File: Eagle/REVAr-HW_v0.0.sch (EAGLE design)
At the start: 104 parts, among them IC1 MC33269ST-5.0T3, IC2 MC33269D-5.0, IC3 ATMEGA2560-16AU, IC4 ATMEGA8U2-MU, IC5 LM358D, IC6 LP2985-33DBVR, IC7 PCF8574T, Q1 16MHz, Q2 16MHz, T2 FDN340P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

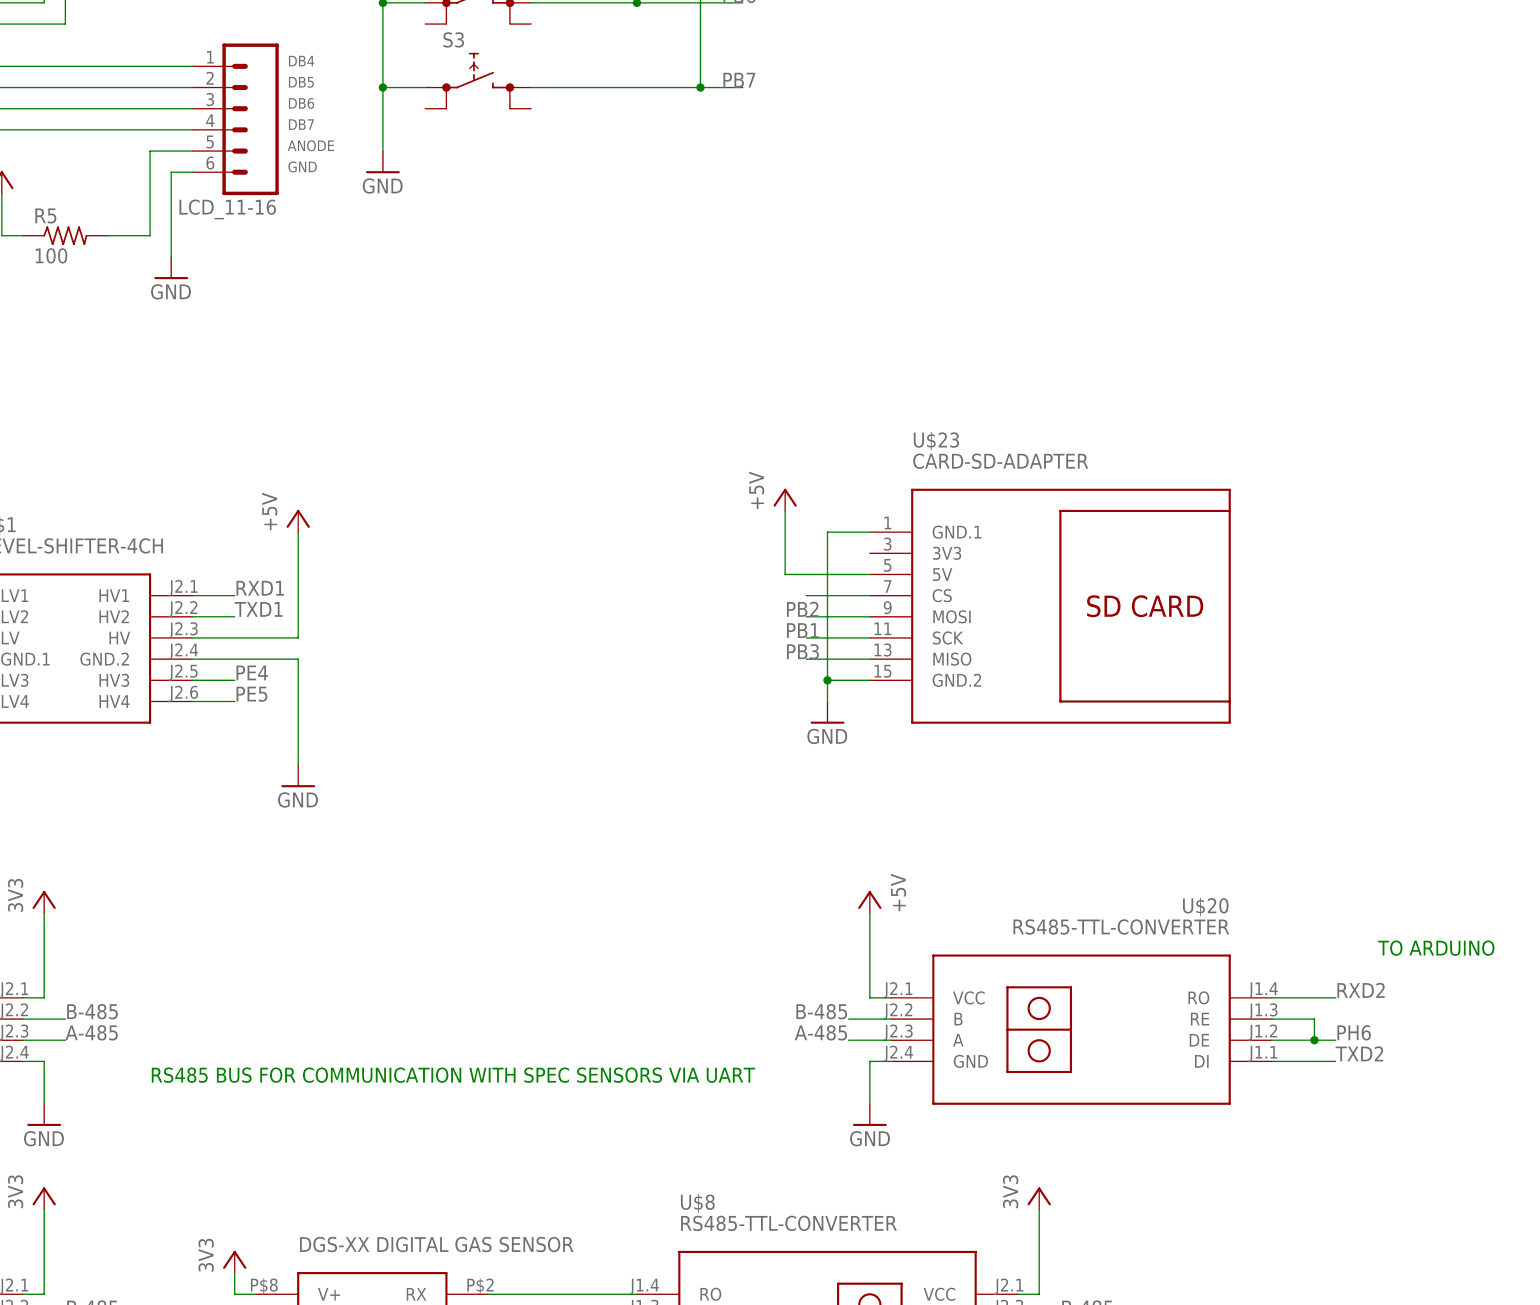
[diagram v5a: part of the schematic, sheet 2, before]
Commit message: [HW] Add BMP280 and DS1307 to design
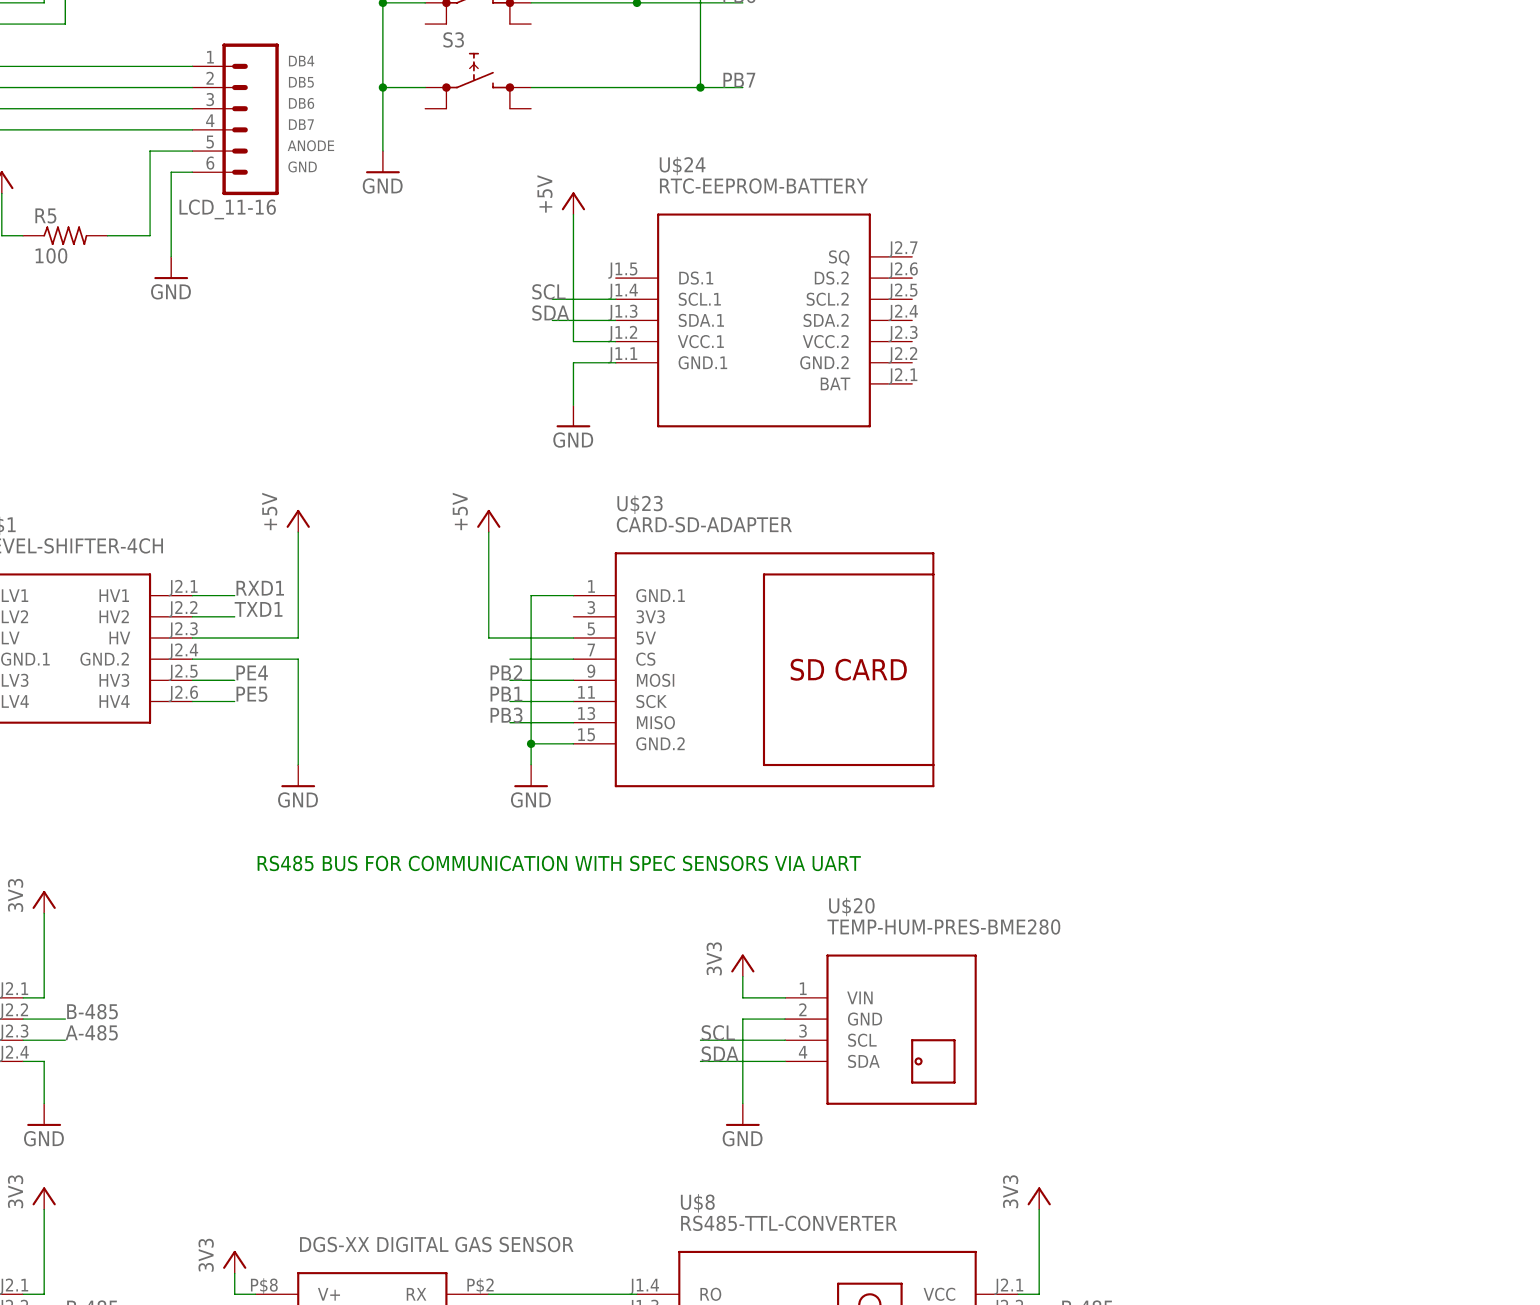
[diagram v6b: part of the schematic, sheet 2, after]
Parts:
- added U$24: RTC-EEPROM-BATTERY, diy-modules:RTC-EEPROM-BATTERY
- added U$25: RS485-TTL-CONVERTER, diy-modules:RS485-TTL-CONVERTER
- U$20: value RS485-TTL-CONVERTER -> TEMP-HUM-PRES-BME280; device diy-modules:RS485-TTL-CONVERTER -> diy-modules:TEMP-HUM-PRES-BME280
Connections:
- net A-485: now also U$25.A; no longer U$20.A
- net B-485: now also U$25.B; no longer U$20.B
- net GND: now also U$24.GND.1, U$25.GND
- net PH6: now also U$25.DE, U$25.RE; no longer U$20.DE, U$20.RE
- net RXD2: now also U$25.RO; no longer U$20.RO
- net SCL: now also U$20.SCL, U$24.SCL.1
- net SDA: now also U$20.SDA, U$24.SDA.1
- net TXD2: now also U$25.DI; no longer U$20.DI
- net VCC: now also U$20.VIN, U$24.VCC.1, U$25.VCC; no longer U$20.VCC
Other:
- note removed: "TO ARDUINO"
- moved on the sheet: U$23
